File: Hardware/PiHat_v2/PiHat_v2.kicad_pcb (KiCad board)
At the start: 2 copper layers, 64 x 55 mm, 35 parts, among them P1 RPiGPIO, P2 CONN_01X02, P3 CONN_01X08

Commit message: Silkscreen Finalized Pending Review
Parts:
- added G***: LOGO, .pretty:makerspace_4,8mm, B.Cu at (122.0, 89.5)
- added G***: LOGO, .pretty:ci_wide_6mm, B.Cu at (104.8, 89.2)
- added G***: LOGO, .pretty:tiger_paw_10mm, B.Cu at (143.0, 89.5)
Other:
- board text added: "Stefan Abare - Giandre Acosta - Maurice Barnett Thor Brockman - Brice Grooms - Brad Hord Joshua McMillan - Owen Phillips - Garrett Ross"
- board text removed: "Stefan Abare Giandre Acosta Maurice Barnett Thor Brockman Brice Grooms Brad Hord Joshua McMillan Owen Phillips Garrett Ross"

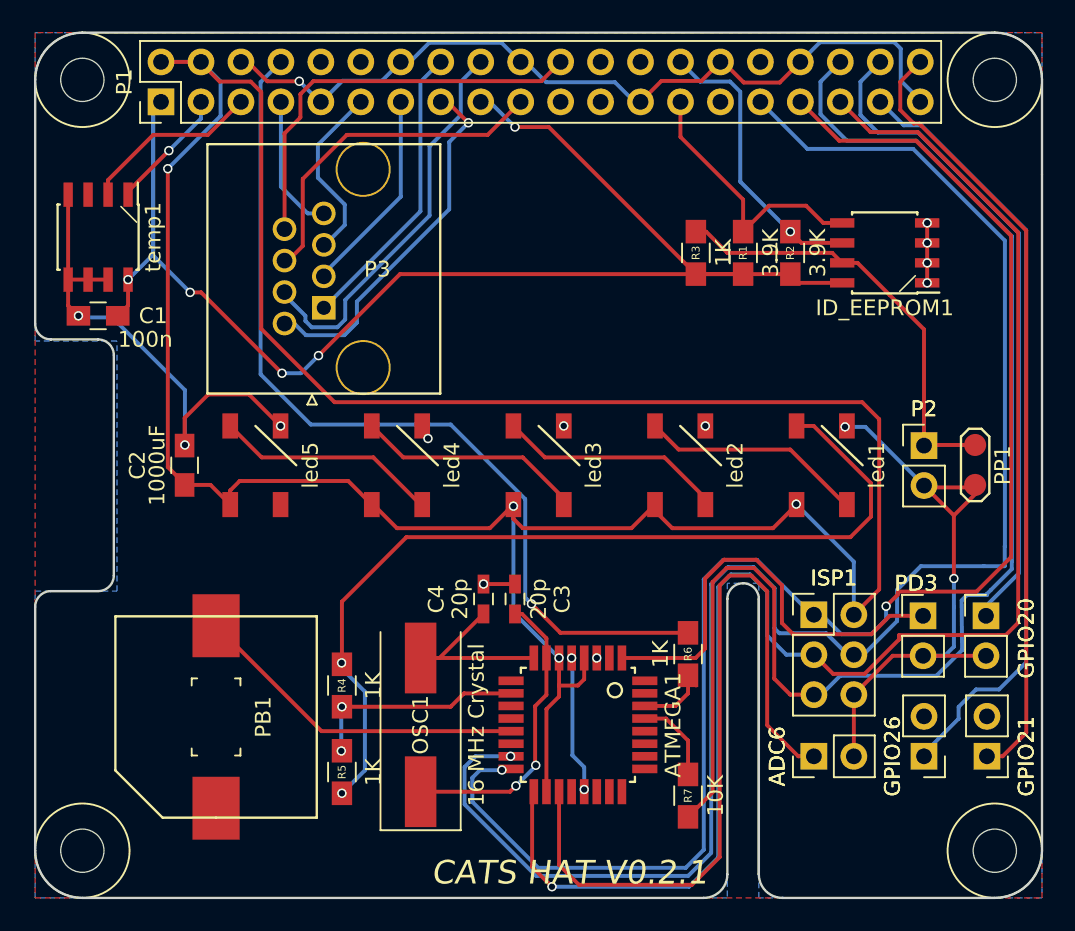
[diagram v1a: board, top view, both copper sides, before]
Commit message: Pi Hat - now with non-imaginary components (#155)
* Adjust Silkscreen Layout on PCB

* Add 1000uF AluCap Footprint & Rename 100nF to 0.1uF

* Implement AluCap in PCB

* Connect New Keypad GPIO Schema

* Built the BOM

* Move Silkscreen Logo

* YASA - Yet Another Silkscreen Adjustment

* Update Version Number of PiHat

* Rotate AluCap for Proper Polarity

* Fix BOM Whitespace
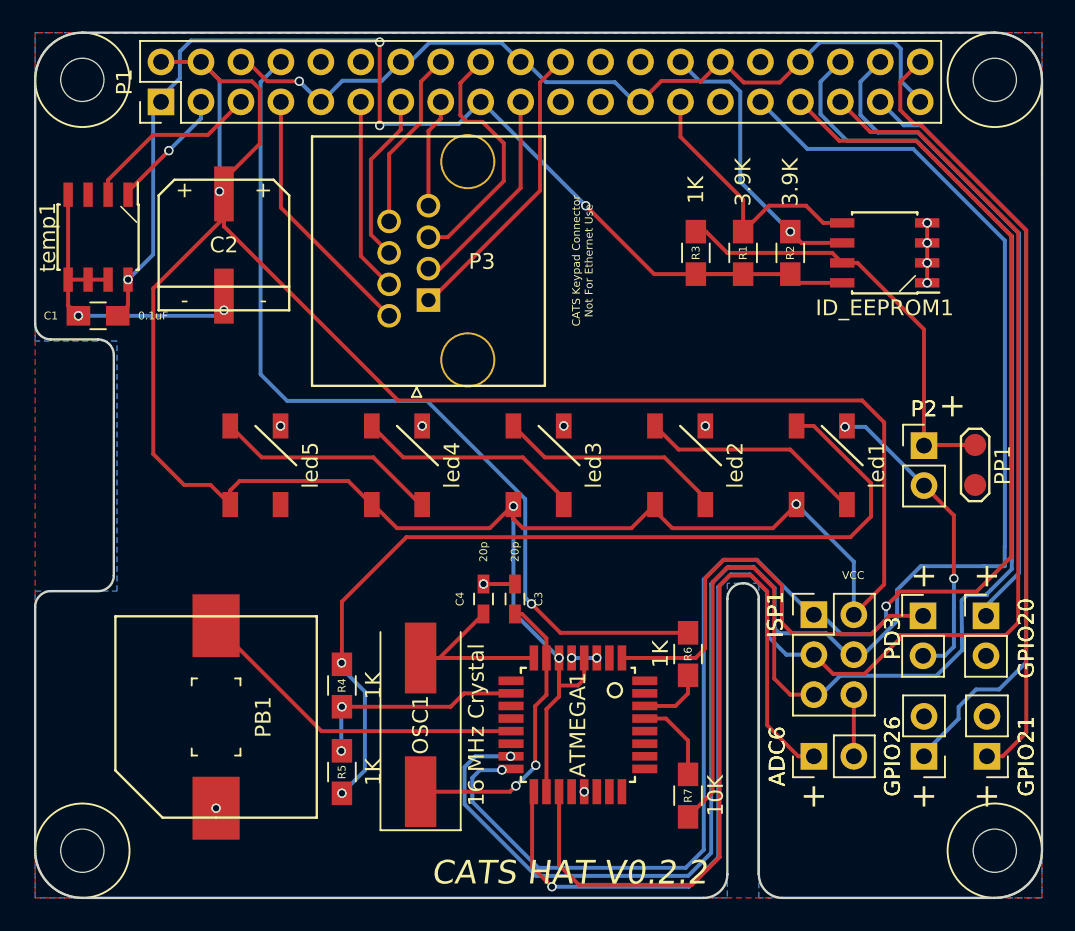
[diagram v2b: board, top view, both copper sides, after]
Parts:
- C1: value 100n -> 0.1uF
- C2: footprint Capacitors_SMD:C_0805_HandSoldering -> .pretty:AluCap_8mmDia_Nichicon
- moved C2 14.2 mm to (106.0, 75.5), turned to 0 degrees
- moved G*** 10.0 mm to (112.0, 89.5)
- moved P3 6.67 mm to (119.0, 79.0)
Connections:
- C2 pad 1: GND -> +5V
- C2 pad 2: +5V -> GND
- P3 pad 1: /GPIO23 -> /GPIO25
- P3 pad 2: /GPIO22 -> /GPIO4
- P3 pad 3: /GPIO27 -> /GPIO10
- P3 pad 4: /GPIO24 -> /GPIO17
- P3 pad 5: /GPIO17 -> /GPIO24
- P3 pad 6: /GPIO10 -> /GPIO27
- P3 pad 7: /GPIO4 -> /GPIO22
- P3 pad 8: /GPIO25 -> /GPIO23
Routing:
- net GND: track 139.9 -> 105.4 mm, vias 18 -> 19
- net +3V3: track 95.7 -> 75.3 mm, vias 5 -> 4
- net /GPIO22: track 23.2 -> 7.35 mm, vias 1 -> 0
- net /GPIO24: track 25.2 -> 16.1 mm
- net /GPIO10: track 21.8 -> 13.5 mm
- net /GPIO25: track 26.4 -> 18.7 mm
- net /GPIO4: track 8.82 -> 16.4 mm
- net /GPIO23: track 18.7 -> 11.5 mm
- net /GPIO27: track 13.1 -> 10.9 mm
- net Net-(ATMEGA1-Pad30): track 4.88 -> 4.23 mm
- net +5V: track 186.2 -> 185.7 mm
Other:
- board text added: "+"
- board text added: "CATS HAT V0.2.2"
- board text added: "CATS Keypad Connector Not For Ethernet Use"
- board text added: "VCC"
- board text removed: "CATS HAT V0.2.1"

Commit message: Connect GPIO RX and ATMega TX - Enlarge select silkscreen graphics
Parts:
- removed G***: LOGO, .pretty:makerspace_4,8mm
- removed G***: LOGO, .pretty:ci_wide_6mm
- removed G***: LOGO, .pretty:tiger_paw_10mm
- added R6: 1K, .pretty:R_0805_HandSoldering, F.Cu at (131.5, 97.1)
- renumbered R6 to R7, R7 to R8, P2 to WP
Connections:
- P1 pad 10: Net-(P1-Pad10) -> /UART_RXD
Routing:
- net /UART_RXD: track 0.00 -> 42.3 mm, vias 0 -> 2
- net Net-(ATMEGA1-Pad31): track 0.00 -> 7.07 mm, vias 0 -> 2
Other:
- board text added: "5V"
- board text added: "GPIO RX"
- board text added: "GPIO TX"
- board text removed: "VCC"
